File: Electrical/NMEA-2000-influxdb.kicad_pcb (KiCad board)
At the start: 4 copper layers, 114.3 x 71.1 mm, 10 parts, among them J1 Conn_01x04, J2 Conn_01x04, U1 SD-Card-Module, U2 LM7805_TO220, U3 ESP32_NODEMCU, U4 SN65HVD230, U5 RTC-Module

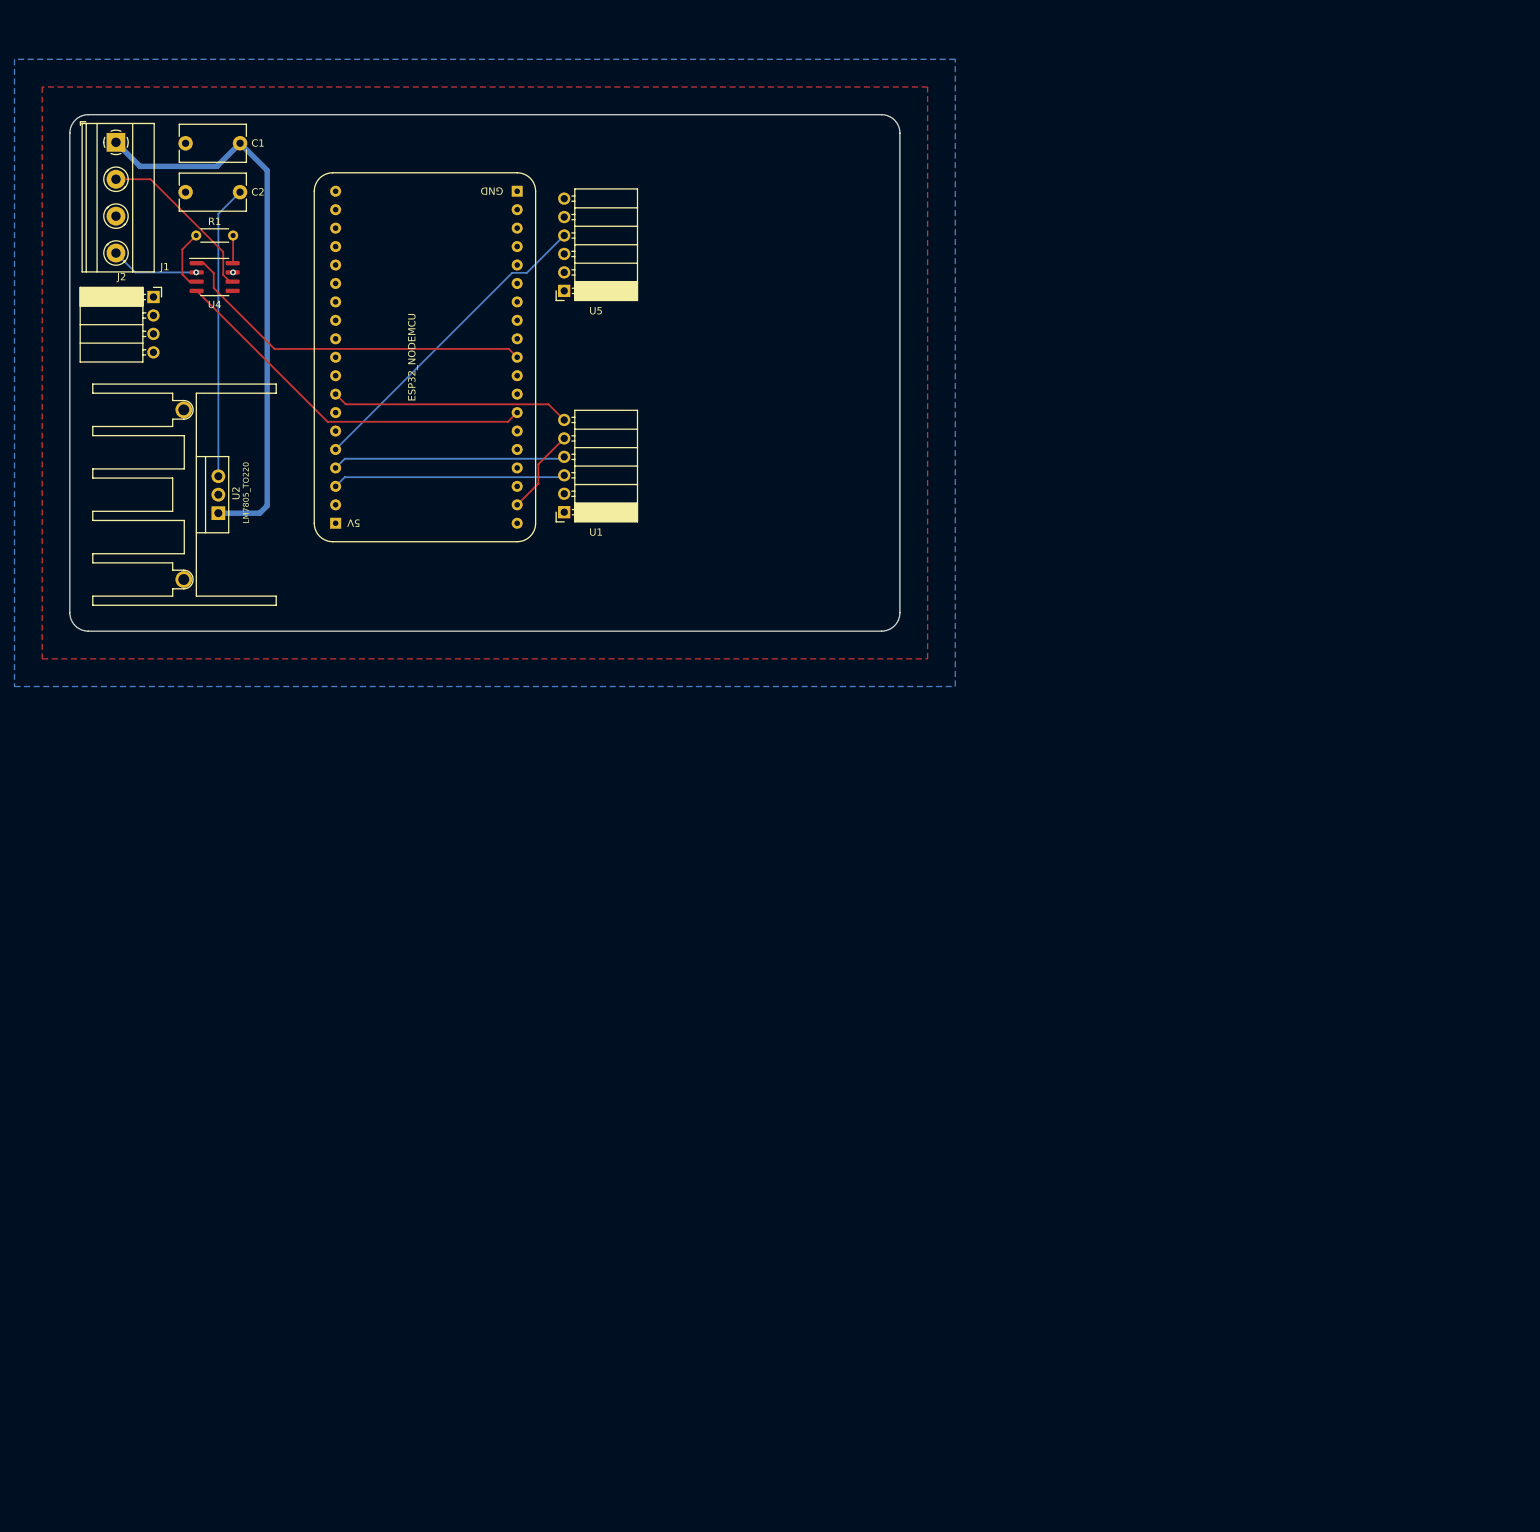
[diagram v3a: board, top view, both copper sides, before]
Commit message: Added Display PCB
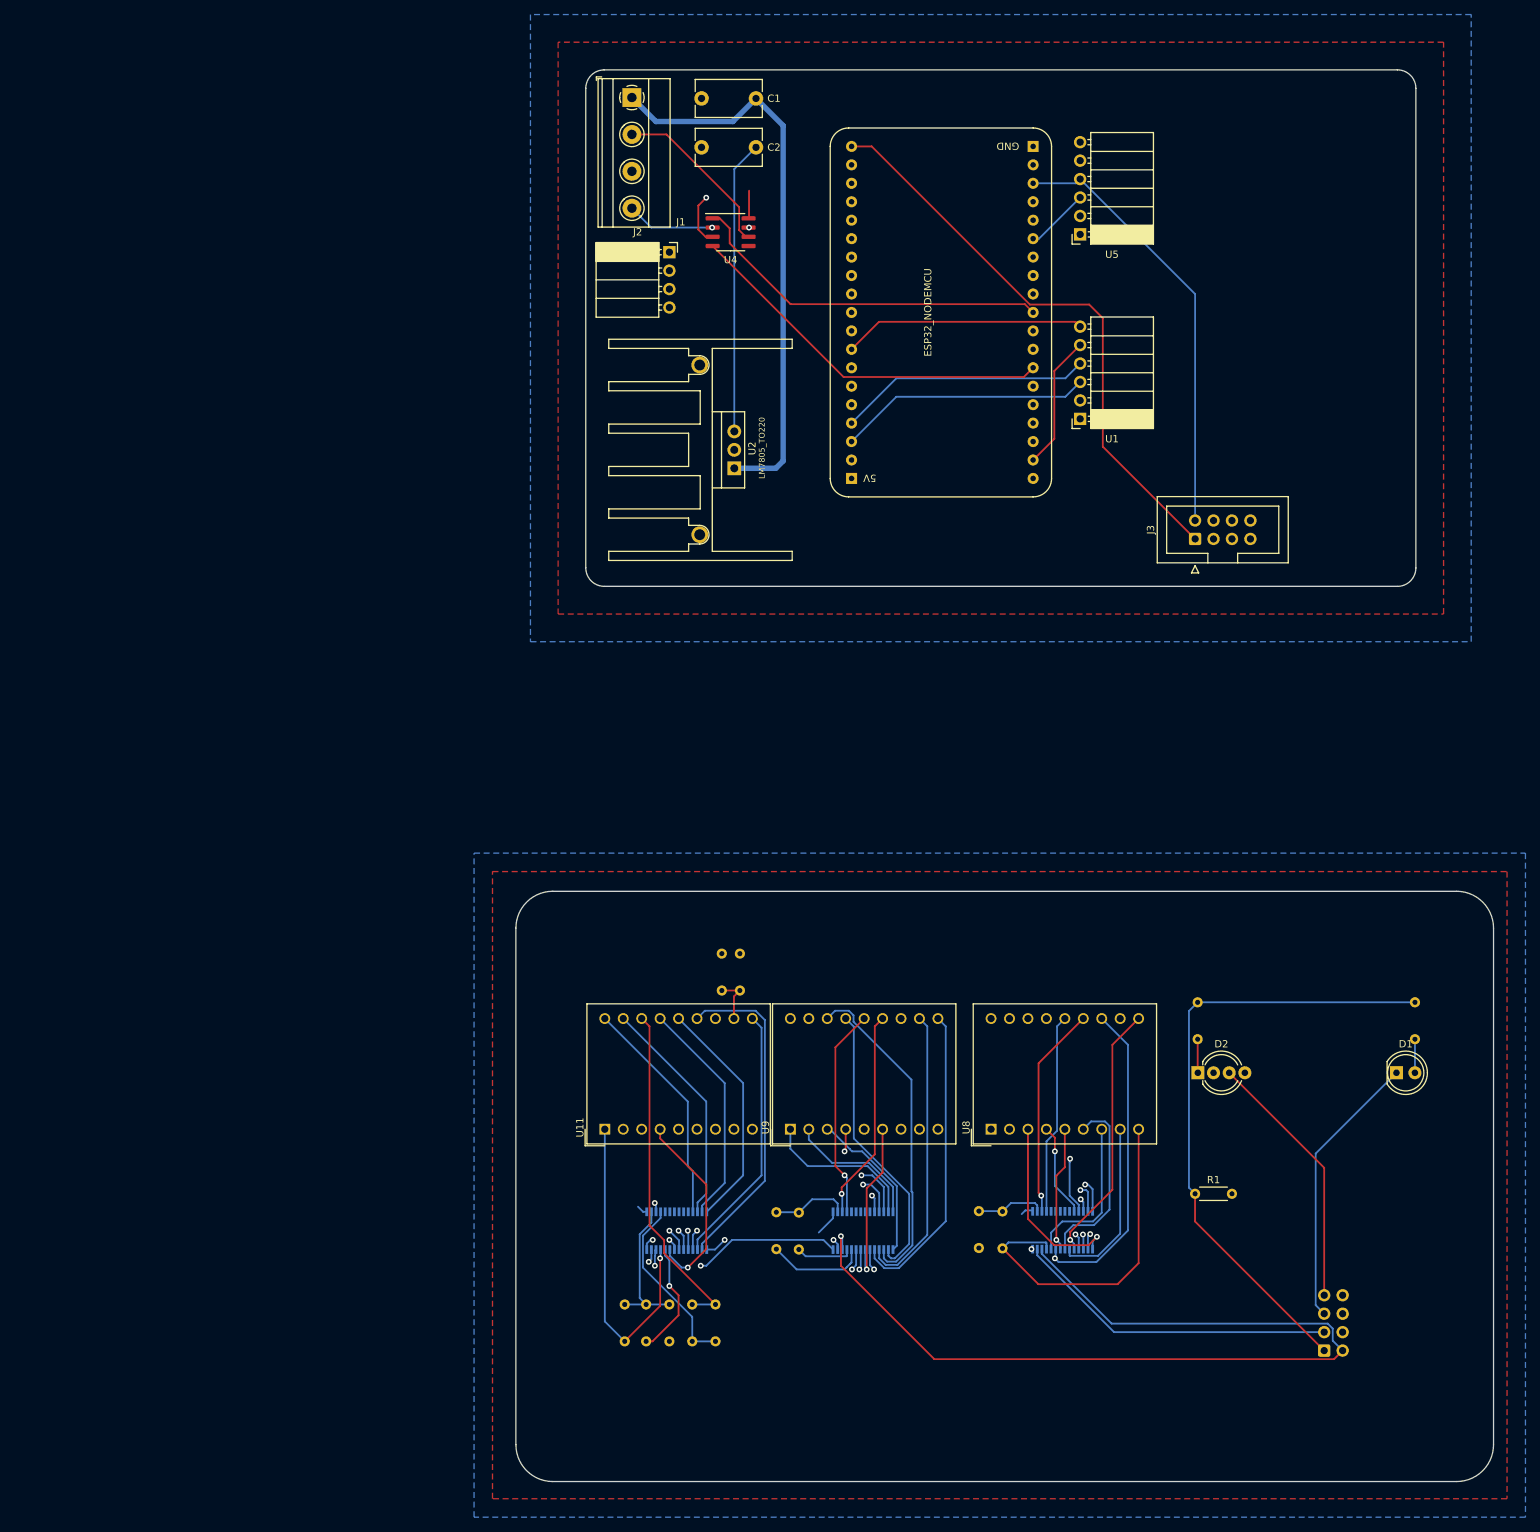
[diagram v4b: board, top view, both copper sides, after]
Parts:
- added D1: LED, LED_THT:LED_D5.0mm, F.Cu at (274.1, 170.0)
- added D2: LED_ABGR, LED_THT:LED_D5.0mm-4_RGB_Wide_Pins, F.Cu at (246.8, 170.0)
- added J3: Conn_02x04_Top_Bottom, Connector_IDC:IDC-Header_2x04_P2.54mm_Vertical, F.Cu at (246.4, 96.5)
- added J4: Conn_02x04_Top_Bottom, Connector_IDC:IDC-Header_2x04_P2.54mm_Vertical, B.Cu at (264.2, 208.3)
- added R1: 38k, Resistor_THT:R_Axial_DIN0204_L3.6mm_D1.6mm_P5.08mm_Horizontal, B.Cu at (219.9, 189.1)
- added R10: 22R, Resistor_THT:R_Axial_DIN0204_L3.6mm_D1.6mm_P5.08mm_Horizontal, B.Cu at (177.1, 207.0)
- added R11: 22R, Resistor_THT:R_Axial_DIN0204_L3.6mm_D1.6mm_P5.08mm_Horizontal, B.Cu at (180.3, 207.0)
- added R12: R, Resistor_THT:R_Axial_DIN0204_L3.6mm_D1.6mm_P5.08mm_Horizontal, B.Cu at (276.7, 160.3)
- added R13: R, Resistor_THT:R_Axial_DIN0204_L3.6mm_D1.6mm_P5.08mm_Horizontal, B.Cu at (246.7, 160.3)
- added R2: 38k, Resistor_THT:R_Axial_DIN0204_L3.6mm_D1.6mm_P5.08mm_Horizontal, B.Cu at (216.6, 189.1)
- added R3: 38k, Resistor_THT:R_Axial_DIN0204_L3.6mm_D1.6mm_P5.08mm_Horizontal, B.Cu at (191.8, 189.3)
- added R4: 38k, Resistor_THT:R_Axial_DIN0204_L3.6mm_D1.6mm_P5.08mm_Horizontal, B.Cu at (188.7, 189.2)
- added R5: 47k, Resistor_THT:R_Axial_DIN0204_L3.6mm_D1.6mm_P5.08mm_Horizontal, B.Cu at (174.0, 201.9)
- added R6: 47k, Resistor_THT:R_Axial_DIN0204_L3.6mm_D1.6mm_P5.08mm_Horizontal, B.Cu at (170.8, 201.9)
- added R7: 47k, Resistor_THT:R_Axial_DIN0204_L3.6mm_D1.6mm_P5.08mm_Horizontal, B.Cu at (167.8, 201.9)
- added R8: 22R, Resistor_THT:R_Axial_DIN0204_L3.6mm_D1.6mm_P5.08mm_Horizontal, B.Cu at (183.7, 153.6)
- added R9: R, Resistor_THT:R_Axial_DIN0204_L3.6mm_D1.6mm_P5.08mm_Horizontal, B.Cu at (181.2, 153.6)
- added U10: ~, Package_SO:SSOP-28_3.9x9.9mm_P0.635mm, B.Cu at (175.0, 191.8)
- added U11: JM-S05422A-001, Display_7Segment:DA56-11CGKWA, F.Cu at (165.1, 177.8)
- added U6: ~, Package_SO:SSOP-28_3.9x9.9mm_P0.635mm, B.Cu at (228.1, 191.7)
- added U7: ~, Package_SO:SSOP-28_3.9x9.9mm_P0.635mm, B.Cu at (200.7, 191.8)
- added U8: DA56-11CGKWA, Display_7Segment:DA56-11CGKWA, F.Cu at (218.3, 177.8)
- added U9: DA56-11CGKWA, Display_7Segment:DA56-11CGKWA, F.Cu at (190.7, 177.8)
- moved R1 190.6 mm to (246.4, 186.7)
- moved U1 72.2 mm to (230.6, 80.0)
- moved U5 71.5 mm to (230.6, 54.6)
- moved C1 71.3 mm to (185.9, 35.9)
- moved C2 71.3 mm to (185.9, 42.6)
- moved J2 71.3 mm to (174.0, 57.0)
- moved U2 71.3 mm to (182.9, 86.8)
- moved U3 71.3 mm to (211.4, 65.3)
- moved J1 71.3 mm to (168.8, 35.7)
- moved U4 71.3 mm to (182.4, 54.3)
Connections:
- U3 pad 23: unconnected-(U3-G15-Pad23) -> /WIFI
- U3 pad 27: unconnected-(U3-G16-Pad27) -> /RED
- U3 pad 28: unconnected-(U3-G17-Pad28) -> /GREEN
- U3 pad 30: unconnected-(U3-G18-Pad30) -> /BLUE
- U3 pad 33: unconnected-(U3-G21-Pad33) -> SDA
- U3 pad 36: unconnected-(U3-G22-Pad36) -> SCL
- U3 pad 5: /SCL -> unconnected-(U3-G13-Pad5)
- U3 pad 7: /SDA -> unconnected-(U3-G12-Pad7)
- U4 pad 3: +3.3V -> +3V3
- U4 pad 8: Net-(U4-Rs) -> GND
- U5 pad 3: /SDA -> SDA
- U5 pad 4: /SCL -> SCL
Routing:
- net /Display/SDA: track 0.00 -> 161.0 mm, vias 0 -> 2
- net /Display/SCL: track 0.00 -> 159.2 mm, vias 0 -> 2
- net +3V3: track 0.00 -> 110.2 mm, vias 0 -> 1
- net +3.3V: track 8.53 -> 86.1 mm
- net SDA: track 0.00 -> 60.5 mm
- net SCL: track 0.00 -> 60.3 mm
- net Net-(U6-ROW2/A0): track 0.00 -> 55.1 mm, vias 0 -> 1
- net Net-(U7-ROW1/A1): track 0.00 -> 50.4 mm
- net Net-(U6-ROW0/A2): track 0.00 -> 47.7 mm
- net Net-(U11-COM2): track 0.00 -> 46.8 mm
- net Net-(U10-ROW1/A1): track 0.00 -> 46.3 mm, vias 0 -> 1
- net /BLUE: track 0.00 -> 45.7 mm
- net Net-(U7-ROW8/K6): track 0.00 -> 45.6 mm
- net Net-(U10-ROW9/K7): track 0.00 -> 45.5 mm
- net Net-(U10-ROW0/A2): track 0.00 -> 45.0 mm, vias 0 -> 1
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- added copper zone on F.Cu, net +5VD
- added copper zone on B.Cu, net GND1
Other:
- board size 114.3 x 71.1 mm -> 134.6 x 194.4 mm

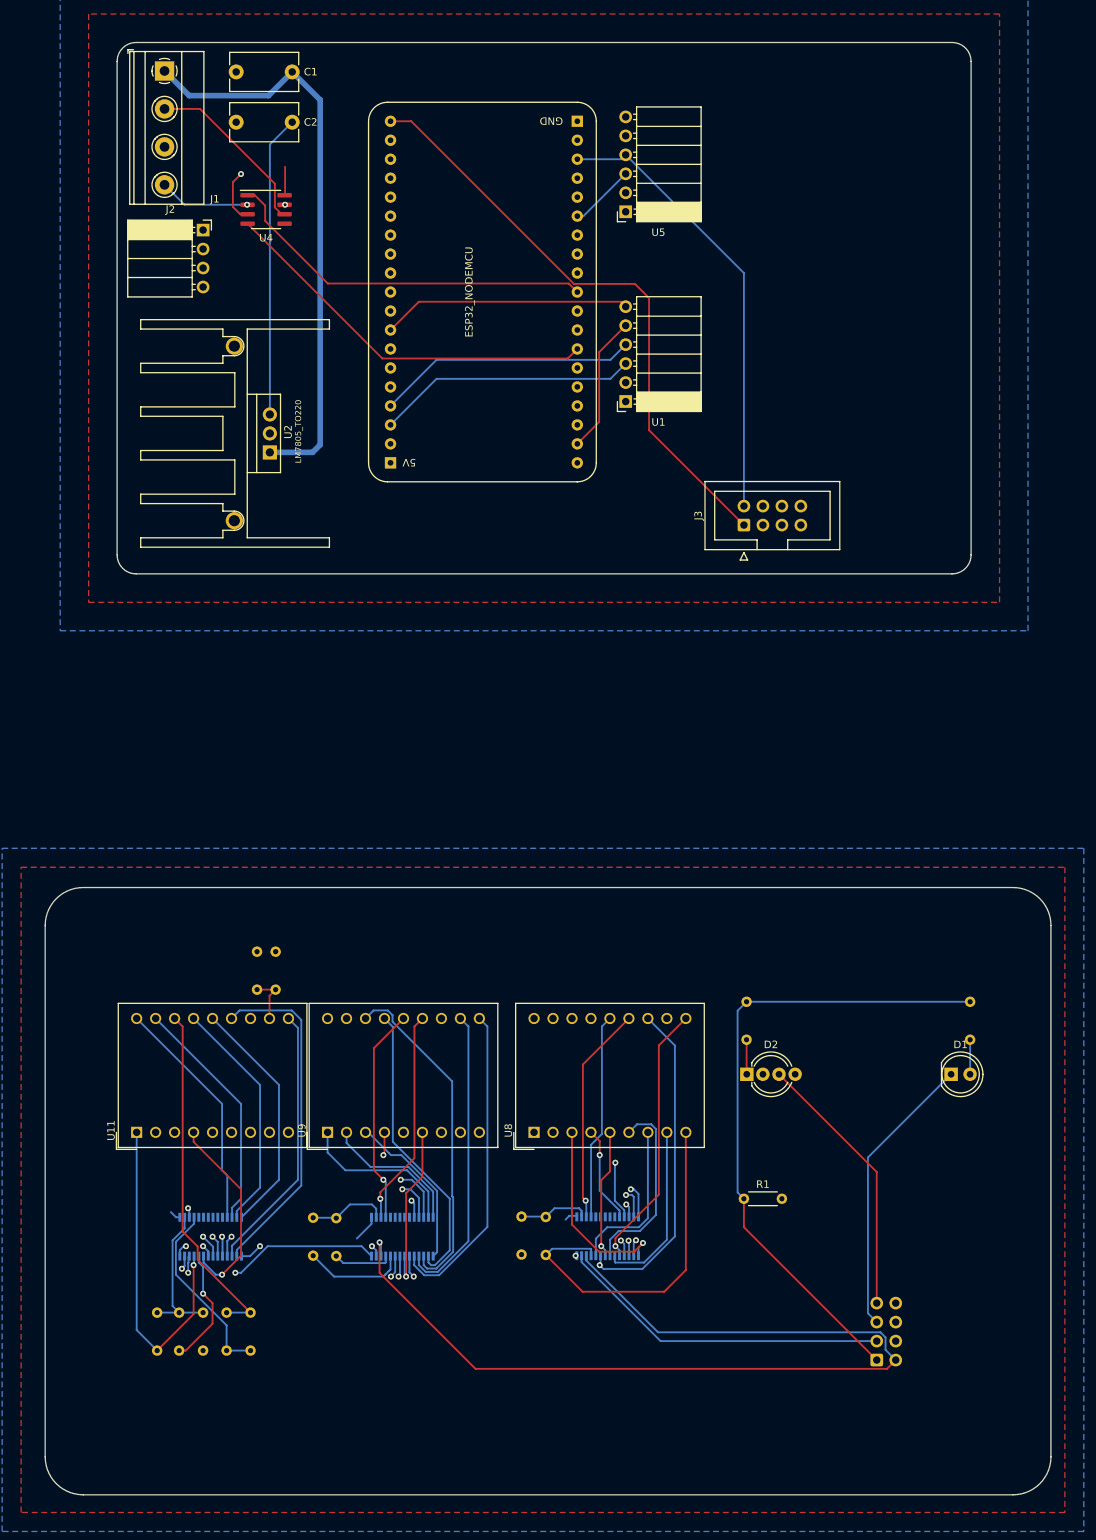
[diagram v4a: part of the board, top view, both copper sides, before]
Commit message: Updated Display
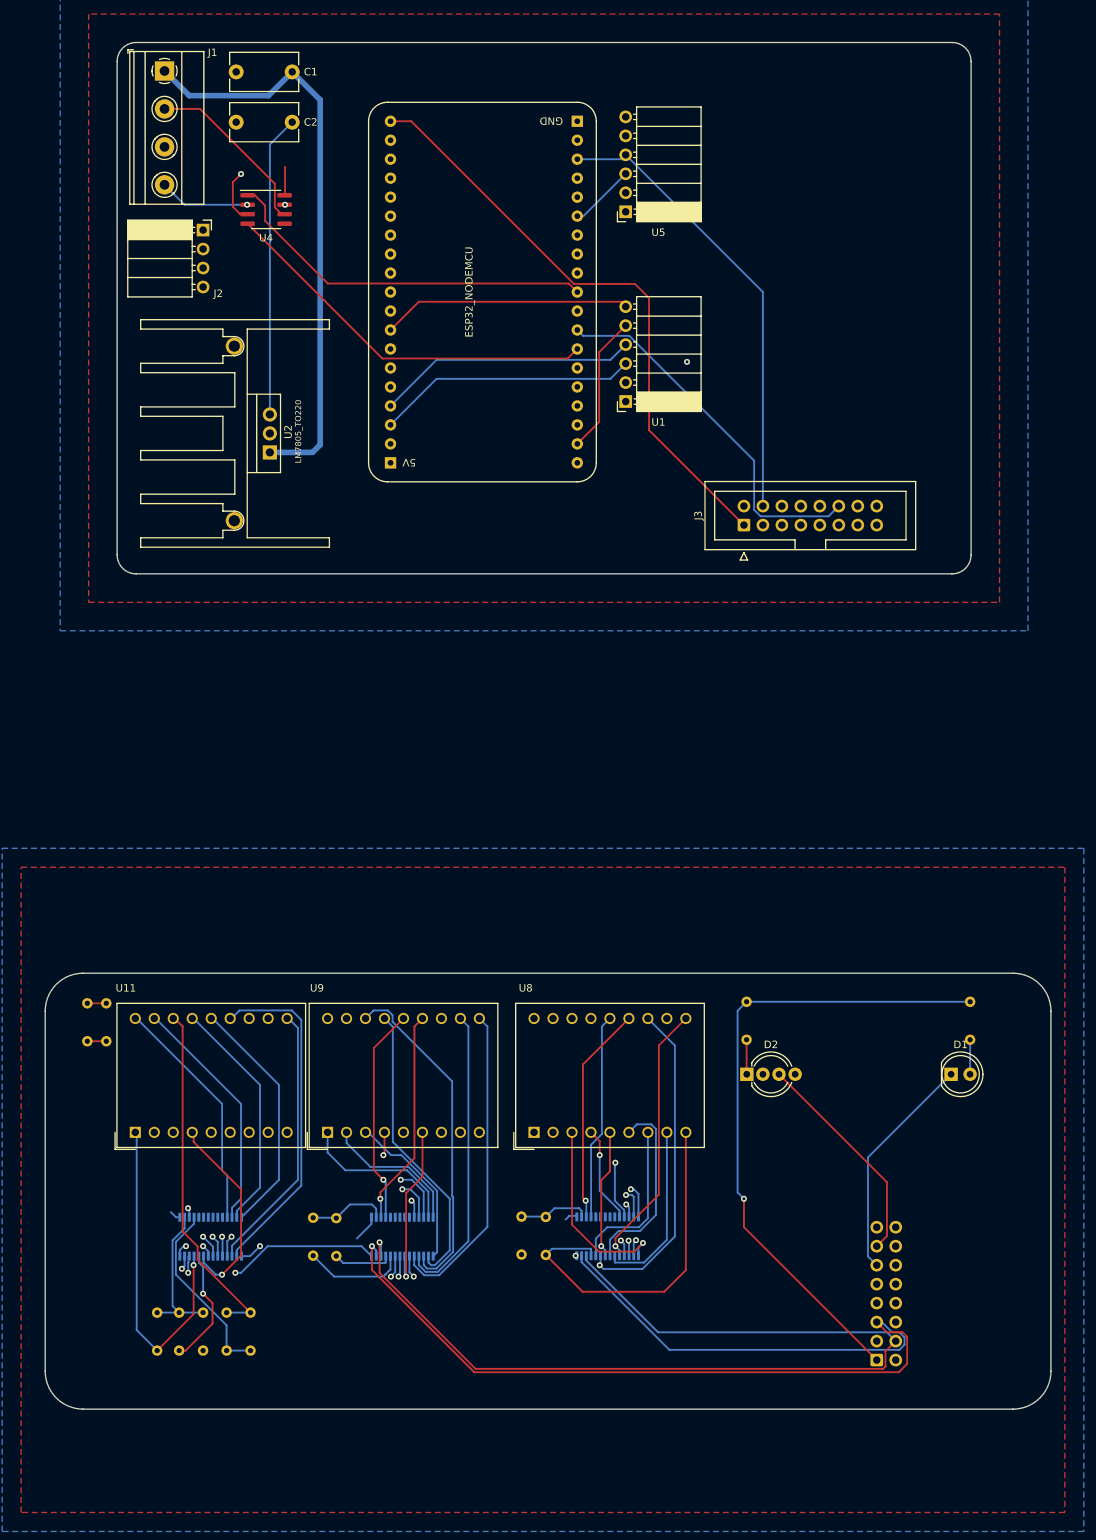
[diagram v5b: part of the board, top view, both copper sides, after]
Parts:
- removed the R1 at (246.4, 186.7)
- J3, J4: footprint Connector_IDC:IDC-Header_2x04_P2.54mm_Vertical -> Connector_IDC:IDC-Header_2x08_P2.54mm_Vertical
- moved R9 25.7 mm to (158.5, 165.6), turned to 90 degrees
- moved R8 25.6 mm to (161.0, 165.6), turned to 90 degrees
- moved U11 0.18 mm to (164.9, 177.8)
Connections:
- J3 pad 2: SCL -> unconnected-(J3-Pin_2-Pad2)
- J3 pad 3: SDA -> unconnected-(J3-Pin_3-Pad3)
- J3 pad 4: GND -> SCL
- J3 pad 5: /WIFI -> SDA
- J3 pad 6: /RED -> unconnected-(J3-Pin_6-Pad6)
- J3 pad 7: /GREEN -> unconnected-(J3-Pin_7-Pad7)
- J3 pad 8: /BLUE -> GND
- J4 pad 2: /Display/SCL -> unconnected-(J4-Pin_2-Pad2)
- J4 pad 3: /Display/SDA -> unconnected-(J4-Pin_3-Pad3)
- J4 pad 4: GND1 -> /Display/SCL
- J4 pad 5: /Display/WIFI -> /Display/SDA
- J4 pad 6: /Display/RED -> unconnected-(J4-Pin_6-Pad6)
- J4 pad 7: /Display/GREEN -> unconnected-(J4-Pin_7-Pad7)
- J4 pad 8: /Display/BLUE -> GND1
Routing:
- net Net-(U11-COM1): track 6.69 -> 25.0 mm
- net /Display/SDA: track 161.0 -> 176.6 mm
- net Net-(U10-COM1/KS0): track 43.6 -> 30.7 mm
- net /RED: track 38.6 -> 49.7 mm
- net +5V: track 40.4 -> 49.7 mm, vias 0 -> 1
- net /Display/WIFI: track 38.3 -> 30.6 mm
- net /WIFI: track 35.0 -> 42.6 mm
- net /Display/RED: track 39.7 -> 32.5 mm
- net /GREEN: track 44.7 -> 51.5 mm
- net /Display/BLUE: track 38.0 -> 31.4 mm
- net /Display/GREEN: track 36.1 -> 29.6 mm
- net /BLUE: track 45.7 -> 50.5 mm
- net SDA: track 60.5 -> 61.5 mm
- net SCL: track 60.3 -> 61.3 mm
- net +3.3V: vias 0 -> 1
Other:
- board size 134.6 x 194.4 mm -> 134.6 x 182.9 mm
